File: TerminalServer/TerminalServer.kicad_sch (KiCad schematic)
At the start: 88 parts, among them J1 RJ45_LED, J2 RJ45_LED, J3 RJ45_LED, J4 RJ45_LED, J5 RJ45_LED, J6 RJ45_LED, J7 USB_C_Receptacle_USB2.0_14P, J8 Barrel_Jack_Switch, U1 PIC32MX795F512L-80x-PT, U2 XR32330EBERTR-F, U3 XR32330EBERTR-F, U4 XR32330EBERTR-F, U5 XR32330EBERTR-F, U6 XR32330EBERTR-F, U7 XR32330EBERTR-F, U8 ESP32-WROOM-32D, U9 TPS82130

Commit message: Progress
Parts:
- added C49, C50: 100nF, Capacitor_SMD:C_0603_1608Metric_Pad1.08x0.95mm_HandSolder, symbol Device:C_Small
- added C51: 10uF, Capacitor_SMD:C_1206_3216Metric, symbol Device:C_Small
- added J9: Conn_PIC_ICSP_ICD, Connector_PinHeader_2.54mm:PinHeader_1x06_P2.54mm_Vertical, symbol Connector:Conn_PIC_ICSP_ICD
- added Y1: SIT8103AI-23-33E-8.00000X, Oscillator:Oscillator_SMD_SiT_PQFN-4Pin_3.2x2.5mm, symbol Oscillator:SiT8008xx-2x-xxE
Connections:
- net GND: now also C49.1, C50.1, C51.1, J9.3 (VSS), Y1.2 (GND)
- net PGM_CLOCK: now also J9.5 (PGC/ICSPCLK)
- net PGM_DATA: now also J9.4 (PGD/ICSPDAT)
- net RESET: now also J9.1 (~{MCLR}/VPP)
- net VDD: now also C49.2, C50.2, C51.2, J9.2 (VDD), Y1.4 (Vdd)
- net CLOCK: now reaches U1.63 (RC12/OSC1/CLK)
- net CLOCK: now also Y1.3 (OUT)
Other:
- note added: "TODO ==== 1. Clock for PIC32 2. ICSP for ESP32 3. Check USB C PD resistors 4. Add I2C EEPROM 5. Passives for ESP32"

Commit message: Almost complete
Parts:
- removed NT1, NT2: NetTie_2, NetTie:NetTie-2_SMD_Pad2.0mm, symbol Device:NetTie_2
- added C52: 100uF/50V, Capacitor_THT:CP_Radial_D8.0mm_P3.50mm, symbol Device:C_Polarized
- added C53: 220uF/16V, Capacitor_THT:CP_Radial_D6.3mm_P2.50mm, symbol Device:C_Polarized
- added C54: 100nF, Capacitor_SMD:C_0603_1608Metric_Pad1.08x0.95mm_HandSolder, symbol Device:C_Small
- added J10: Conn_01x06_Pin, Connector_PinHeader_2.54mm:PinHeader_1x06_P2.54mm_Vertical, symbol Connector:Conn_01x06_Pin
- added LED1: 553-0121F, KiCad:5530121F, symbol 553-0121F:553-0121F
- added R16, R17, R18: 10k, Resistor_SMD:R_0603_1608Metric_Pad0.98x0.95mm_HandSolder, symbol Device:R_Small
- added R19, R20: 100R, Resistor_SMD:R_0603_1608Metric_Pad0.98x0.95mm_HandSolder, symbol Device:R_Small
- added R21, R22: 2k2, Resistor_SMD:R_0603_1608Metric_Pad0.98x0.95mm_HandSolder, symbol Device:R_Small
- added U10: 24LC16, Package_SO:SOIC-8_3.9x4.9mm_P1.27mm, symbol Memory_EEPROM:24LC16
- J8: footprint (none) -> Connector_BarrelJack:BarrelJack_Wuerth_6941xx301002
- J9: now not fitted
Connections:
- net GNDA is gone; now on net GND: C46.1, C47.1, C48.1, R15.2, U9.3 (GND), U9.9 (GND)
- net GND: now also J1.11, J2.11, J2.9, J3.11, J3.9, J4.11, J4.9, J5.11, J5.9, J6.11, J6.9, J8.2, J8.3, C52.2, C53.2, C54.1, J10.3 (Pin_3), LED1.1 (K_1), LED1.3 (K_2), R18.2, U10.1 (A0), U10.2 (A1), U10.3 (A2), U10.4 (GND), U10.7 (WP)
- net SCL: now also R21.1, U10.6 (SCL)
- net SDA: now also R22.1, U10.5 (SDA)
- net VCC: now also C52.1
- net VDD: now also C53.1, C54.2, J10.2 (Pin_2), R16.1, R17.2, R20.1, R21.2, R22.2, U10.8 (VCC)
- net ESP_LED: now reaches U8.23 (IO15)
- net ESP_LED: now also R19.2
- net at U8.24 (IO2): now also R18.1
- net ESP_IO0: now reaches U8.25 (IO0)
- net ESP_IO0: now also J10.6 (Pin_6), R17.1
- net ESP_EN: now reaches U8.3 (EN)
- net ESP_EN: now also J10.1 (Pin_1), R16.2
- net ESP_RX: now reaches U8.34 (RXD0/IO3)
- net ESP_RX: now also J10.5 (Pin_5)
- net ESP_TX: now reaches U8.35 (TXD0/IO1)
- net ESP_TX: now also J10.4 (Pin_4)
- new net: LED1.4 (A_2), R19.1
- new net: LED1.2 (A_1), R20.2
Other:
- note added: "TODO ==== 1. Check USB C PD resistors"
- note removed: "TODO ==== 1. Clock for PIC32 2. ICSP for ESP32 3. Check USB C PD resistors 4. Add I2C EEPROM 5. Passives for ESP32"
- moved on the sheet: H1, H2, H3, H4

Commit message: Added Ethernet and more
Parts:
- removed U8: ESP32-WROOM-32D, RF_Module:ESP32-WROOM-32D, symbol RF_Module:ESP32-WROOM-32D
- added C55: 10uF, Capacitor_SMD:C_0805_2012Metric_Pad1.18x1.45mm_HandSolder, symbol Device:C_Small
- added C56, C57, C58, C59, C60: 100nF, Capacitor_SMD:C_0603_1608Metric_Pad1.08x0.95mm_HandSolder, symbol Device:C_Small
- added D3: 1N5819WS, Diode_SMD:D_SOD-323, symbol Diode:1N5819WS
- added J11: SI-60118-F, SI60118F, symbol SI-60118-F:SI-60118-F
- added J12: Conn_01x08_Pin, Connector_PinHeader_2.54mm:PinHeader_1x08_P2.54mm_Vertical, symbol Connector:Conn_01x08_Pin
- added L1: L_Ferrite, Inductor_SMD:L_0603_1608Metric_Pad1.05x0.95mm_HandSolder, symbol Device:L_Ferrite
- added R23: 10k, Resistor_SMD:R_0603_1608Metric_Pad0.98x0.95mm_HandSolder, symbol Device:R_Small
- added R24: 2k32, Resistor_SMD:R_0603_1608Metric_Pad0.98x0.95mm_HandSolder, symbol Device:R_Small
- added R25, R26, R27, R28: 49R9, Resistor_SMD:R_0603_1608Metric_Pad0.98x0.95mm_HandSolder, symbol Device:R_Small
- added R29, R30: 100R, Resistor_SMD:R_0603_1608Metric_Pad0.98x0.95mm_HandSolder, symbol Device:R_Small
- added SW1: SW_Push, Button_Switch_THT:SW_Tactile_SPST_Angled_PTS645Vx31-2LFS, symbol Switch:SW_Push
- added SW2: SW_SPDT, Button_Switch_THT:SW_Slide_SP3T_Straight_CK_OS103012MU1QP1, symbol Switch:SW_SPDT
- added U11: ENC28J60x-ML, Package_DFN_QFN:QFN-28-1EP_6x6mm_P0.65mm_EP4.25x4.25mm, symbol Interface_Ethernet:ENC28J60x-ML
- added U12: ESP32-S3-WROOM-1, RF_Module:ESP32-S3-WROOM-1, symbol RF_Module:ESP32-S3-WROOM-1
- added Y2: ASEMB-25.000MHZ-LC-T, Oscillator:Oscillator_SMD_SiT_PQFN-4Pin_3.2x2.5mm, symbol Oscillator:SiT8008xx-2x-xxE
- J10: footprint Connector_PinHeader_2.54mm:PinHeader_1x06_P2.54mm_Vertical -> Connector_PinHeader_2.54mm:PinHeader_1x10_P2.54mm_Vertical; symbol Connector:Conn_01x06_Pin -> Connector:Conn_01x10_Pin
- LED1: footprint KiCad:5530121F -> LEDS:5530121F
- Y1: value SIT8103AI-23-33E-8.00000X -> ASEMB-8.000MHZ-LC-T
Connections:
- net WIFI_INT is gone; now on net U3DTR: U1.18 (RE8)
- net WIFI_SEL is gone; now on net U1SHTDN: U1.77 (RD2)
- net ESP_EN: now also U1.17 (RA0/TMS), U12.3 (EN)
- net ESP_IO0: now also U12.27 (IO0)
- net ESP_LED: now also U12.8 (IO15)
- net ESP_RX: now also J10.4 (Pin_4), U12.36 (RXD0); no longer J10.5 (Pin_5)
- net ESP_TX: now also J10.5 (Pin_5), U12.37 (TXD0); no longer J10.4 (Pin_4)
- net GND: now also J10.9 (Pin_9), C55.2, C56.1, C57.1, C58.1, C59.1, C60.1, J11.10 (K_GREEN_1), J11.12 (K_GREEN_2), J11.MH1, J11.MH2, J12.8 (Pin_8), R24.2, SW1.2, U11.14 (VSSTX), U11.17 (VSSPLL), U11.18 (VSSOSC), U11.26 (VSS), U11.7 (VSSRX), U12.1 (GND), U12.40 (GND), U12.41 (GND), Y2.2 (GND)
- net SCL: now also U1.58 (RA2), J12.6 (Pin_6); no longer U1.66 (RA14)
- net SDA: now also U1.59 (RA3), J12.7 (Pin_7); no longer U1.67 (RA15)
- net U1CTS: now also U1.79 (RD12); no longer U1.58 (RA2)
- net U1DSR: now also U1.80 (RD13); no longer U1.51 (RF3)
- net U1DTR: now also U1.81 (RD4); no longer U1.60 (RA4/TDI)
- net U1RTS: now also U1.82 (RD5); no longer U1.61 (RA5/TDO)
- net U1RXLED: now also U1.84 (RD7); no longer U1.95 (RG14/TRD2)
- net U1SHTDN: no longer U1.44 (RB15)
- net U1STATUS: now also U1.78 (RD3); no longer U1.59 (RA3)
- net U1TXLED: now also U1.83 (RD6); no longer U1.96 (RG12/TRD1)
- net U2CTS: now also U1.69 (RD9); no longer U1.38 (RA1//TCK)
- net U2DSR: now also U1.73 (RC13/SOSCI); no longer U1.41 (RB12)
- net U2DTR: now also U1.74 (RC14/SOSCO); no longer U1.42 (RB13)
- net U2RTS: now also U1.76 (RD1); no longer U1.43 (RB14)
- net U2RXLED: now also U1.88 (RF1); no longer U1.93 (RE0)
- net U2SHTDN: now also U1.51 (RF3); no longer U1.34 (RB10)
- net U2STATUS: now also U1.68 (RD8); no longer U1.35 (RB11)
- net U2TXLED: now also U1.87 (RF0); no longer U1.94 (RE1)
- net U3CTS: now also U1.7 (RC2); no longer U1.6 (RC1)
- net U3DSR: now also U1.8 (RC3); no longer U1.7 (RC2)
- net U3DTR: no longer U1.8 (RC3)
- net U3RTS: now also U1.19 (RE9); no longer U1.23 (RB2)
- net U3RXLED: now also U1.94 (RE1); no longer U1.87 (RF0)
- net U3SHTDN: now also U1.5 (RE7); no longer U1.4 (RE6)
- net U3STATUS: now also U1.6 (RC1); no longer U1.5 (RE7)
- net U3TXLED: now also U1.93 (RE0); no longer U1.88 (RF1)
- net U4CTS: now also U1.32 (RB8); no longer U1.28 (RA9)
- net U4DSR: now also U1.33 (RB9); no longer U1.29 (RA10)
- net U4DTR: now also U1.34 (RB10); no longer U1.32 (RB8)
- net U4RTS: now also U1.35 (RB11); no longer U1.33 (RB9)
- net U4RXLED: now also U1.90 (RG0); no longer U1.91 (RA6/TRCLK)
- net U4SHTDN: now also U1.28 (RA9); no longer U1.26 (PGEC2/RB6)
- net U4STATUS: now also U1.29 (RA10); no longer U1.27 (PGED2/RB7)
- net U4TXLED: now also U1.89 (RG1); no longer U1.92 (RA7/TRD3)
- net U5CTS: now also U1.22 (RB3); no longer U1.19 (RE9)
- net U5DSR: now also U1.23 (RB2); no longer U1.20 (RB5)
- net U5DTR: now also U1.26 (PGEC2/RB6); no longer U1.21 (RB4)
- net U5RTS: now also U1.27 (PGED2/RB7); no longer U1.22 (RB3)
- net U5RXLED: now also U1.92 (RA7/TRD3); no longer U1.89 (RG1)
- net U5SHTDN: now also U1.20 (RB5); no longer U1.17 (RA0/TMS)
- net U5STATUS: now also U1.21 (RB4); no longer U1.76 (RD1)
- net U5TXLED: now also U1.91 (RA6/TRCLK); no longer U1.90 (RG0)
- net U6DTR: now also U1.3 (RE5); no longer U1.1 (RG15)
- net U6RTS: now also U1.4 (RE6); no longer U1.3 (RE5)
- net U6RXLED: now also U1.96 (RG12/TRD1); no longer U1.83 (RD6)
- net U6TXLED: now also U1.95 (RG14/TRD2); no longer U1.84 (RD7)
- net VCC: now also D3.1 (K), SW2.2 (B); no longer D1.1 (K), D2.1 (K)
- net VDD: now also C58.2, C59.2, C60.2, J12.1 (Pin_1), L1.1, R23.1, U11.11 (VDDTX), U11.15 (VDDRX), U11.16 (VDDPLL), U11.21 (VDDOSC), U11.24 (VDD), U12.2 (3V3), Y2.4 (Vdd)
- net at R18.1: now also U12.16 (IO46)
- net ESP_SEL: now reaches U1.71 (RD11)
- net ESP_SEL: now also U12.19 (IO11)
- net SCK renamed SPI_SCK
- net SPI_SCK: now also U11.4 (SCK), U12.20 (IO12)
- net SDI renamed SPI_MISO
- net SPI_MISO: now also U11.2 (SO), U12.22 (IO14)
- net SDO renamed SPI_MOSI
- net SPI_MOSI: now also U11.3 (SI), U12.18 (IO10)
- net USB_DM renamed USBD_M
- net USB_DP renamed USBD_P
- new net: U11.19 (OSC1), Y2.3 (OUT)
- new net: C55.1, U11.25 (VCAP)
- new net: J11.9 (A_GREEN_1), R29.1
- new net: J11.11 (A_GREEN_2), R30.1
- new net: D3.2 (A), J10.10 (Pin_10)
- new net: R24.1, U11.10 (RBIAS)
- new net ELEDA: R29.2, U11.23 (LEDA)
- new net ELEDB: R30.2, U11.22 (LEDB)
- new net ENC_INT: U1.67 (RA15), U11.28 (~{INT})
- new net ENC_RESET: U1.61 (RA5/TDO), U11.6 (~{RESET})
- new net ENC_SEL: U1.60 (RA4/TDI), U11.5 (~{CS})
- new net ERX_C: C57.2, R27.1, R28.2
- new net ERX_N: J11.6 (RD-), R28.1, U11.8 (TPIN-)
- new net ERX_P: J11.4 (RD+), R27.2, U11.9 (TPIN+)
- new net ESP_INT: U1.66 (RA14), U12.21 (IO13)
- new net ESP_USB_N: J10.8 (Pin_8), U12.13 (USB_D-)
- new net ESP_USB_P: J10.7 (Pin_7), U12.14 (USB_D+)
- new net ETX_C: C56.2, J11.2 (TCT), L1.2, R25.2, R26.1
- new net ETX_N: J11.3 (TD-), R25.1, U11.12 (TPOUT-)
- new net ETX_P: J11.1 (TD+), R26.2, U11.13 (TPOUT+)
- new net FRES: R23.2, SW1.1, U1.1 (RG15)
- new net GPIO0: J12.2 (Pin_2), U1.41 (RB12)
- new net GPIO1: J12.3 (Pin_3), U1.42 (RB13)
- new net GPIO2: J12.4 (Pin_4), U1.43 (RB14)
- new net GPIO3: J12.5 (Pin_5), U1.38 (RA1//TCK)
- new net SWIN: D1.1 (K), D2.1 (K), SW2.3 (C)
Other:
- moved on the sheet: J9, R16, R17, R18

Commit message: Added 4-led module
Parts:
- removed LED1: 553-0121F, LEDS:5530121F, symbol 553-0121F:553-0121F
- removed R19, R20: 100R, Resistor_SMD:R_0603_1608Metric_Pad0.98x0.95mm_HandSolder, symbol Device:R_Small
- added D4: XL-DZ234SYGD-4, XINGLIGHT:XL-DZ234SYGD-4, symbol XINGLIGHT:XL-DZ234SYGD/4
- added R31, R32, R33, R34: 100R, Resistor_SMD:R_0603_1608Metric_Pad0.98x0.95mm_HandSolder, symbol Device:R_Small
- J10: value Conn_01x06_Pin -> Conn_01x10_Pin
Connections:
- net GND: now also D4.1 (LED_K1), D4.3 (LED_K2), D4.5 (LED_K3), D4.7 (LED_K4)
- net LED2: now reaches U12.10 (IO17)
- net LED2: now also R32.1
- net LED3: now reaches U12.11 (IO18)
- net LED3: now also R33.1
- net LED4: now reaches U12.12 (IO8)
- net LED4: now also R34.1
- net LED1: now reaches U12.9 (IO16)
- net LED1: now also R31.1
- new net: D4.2 (LED_A1), R31.2
- new net: D4.4 (LED_A2), R32.2
- new net: D4.6 (LED_A3), R33.2
- new net: D4.8 (LED_A4), R34.2

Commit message: Almost complete
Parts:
- D1, D2, D3: value 1N5819WS -> V8PAN50-M3/I; footprint Diode_SMD:D_SOD-323 -> Diode_SMD:Vishay_SMPA
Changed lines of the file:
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@@
 			)
 		)
-		(property "Value" "1N5819WS"
+		(property "Value" "V8PAN50-M3/I"
 			(at 82.8675 266.7 0)
 			(effects
@@
 			)
 		)
-		(property "Footprint" "Diode_SMD:D_SOD-323"
+		(property "Footprint" "Diode_SMD:Vishay_SMPA"
 			(at 82.55 274.955 0)
 			(effects
@@
 			)
 		)
-		(property "Value" "1N5819WS"
+		(property "Value" "V8PAN50-M3/I"
 			(at 211.1375 232.41 0)
 			(effects
@@
 			)
 		)
-		(property "Footprint" "Diode_SMD:D_SOD-323"
+		(property "Footprint" "Diode_SMD:Vishay_SMPA"
 			(at 210.82 240.665 0)
 			(effects
@@
 			)
 		)
-		(property "Value" "1N5819WS"
+		(property "Value" "V8PAN50-M3/I"
 			(at 108.2675 210.82 0)
 			(effects
@@
 			)
 		)
-		(property "Footprint" "Diode_SMD:D_SOD-323"
+		(property "Footprint" "Diode_SMD:Vishay_SMPA"
 			(at 107.95 219.075 0)
 			(effects

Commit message: Added SD card
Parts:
- added J13: Micro_SD_Card, MolexSD:503182-1852_MOL, symbol Connector:Micro_SD_Card
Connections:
- net ESP_USB_N: now also J10.7 (Pin_7); no longer J10.8 (Pin_8)
- net ESP_USB_P: now also J10.8 (Pin_8); no longer J10.7 (Pin_7)
- net GND: now also J13.6 (VSS)
- net SPI_MISO: now also J13.7 (DAT0)
- net SPI_MOSI: now also J13.3 (CMD)
- net SPI_SCK: now also J13.5 (CLK)
- net VDD: now also J13.4 (VDD)
- net SD_CS: now reaches U1.44 (RB15)
- net SD_CS: now also J13.2 (DAT3/CD)

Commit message: Final cleanup
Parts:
- removed D4: XL-DZ234SYGD-4, XINGLIGHT:XL-DZ234SYGD-4, symbol XINGLIGHT:XL-DZ234SYGD/4
- removed J13: Micro_SD_Card, MolexSD:503182-1852_MOL, symbol Connector:Micro_SD_Card
- removed J7: USB_C_Receptacle_USB2.0_14P, Connector_USB:USB_C_Receptacle_GCT_USB4105-xx-A_16P_TopMnt_Horizontal, symbol Connector:USB_C_Receptacle_USB2.0_14P
- removed R34: 100R, Resistor_SMD:R_0603_1608Metric_Pad0.98x0.95mm_HandSolder, symbol Device:R_Small
- added D4: 564-0100-132F, 5640100222F, symbol 564-0100-132F:564-0100-132F
- added J13: 503398-1892, 5033981892, symbol 503398-1892:503398-1892
- added J7: USB_B, Connector_USB:USB_B_OST_USB-B1HSxx_Horizontal, symbol Connector:USB_B
- U1: Mouser (none) -> 579-PIC32MX795F512
- U2, U3, U4, U5, U6, U7: Mouser (none) -> 701-XR32330EBERTR-F
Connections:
- net GND: now also D4.1 (K_POSITION_3), D4.3 (K_POSITION_2), D4.5 (K_POSITION_1), J13.11, J13.12, J13.13, J13.14, J13.6 (VSS), J7.4 (GND), J7.SH (Shield)
- net SD_CS: now also J13.2 (CD/DAT3)
- net SPI_MISO: now also J13.7 (DAT0)
- net SPI_MOSI: now also J13.3 (CMD)
- net SPI_SCK: now also J13.5 (CLK)
- net USBD_M: now also J7.2 (D-)
- net USBD_P: now also J7.3 (D+)
- net USB_VBUS: now also J7.1 (VBUS)
- net VDD: now also J13.4 (VDD)
- net at R31.2: now also D4.2 (A_POSITION_3)
- net at R32.2: now also D4.4 (A_POSITION_2)
- net at R33.2: now also D4.6 (A_POSITION_1)
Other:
- moved on the sheet: C52, D1, R31, R32, R33

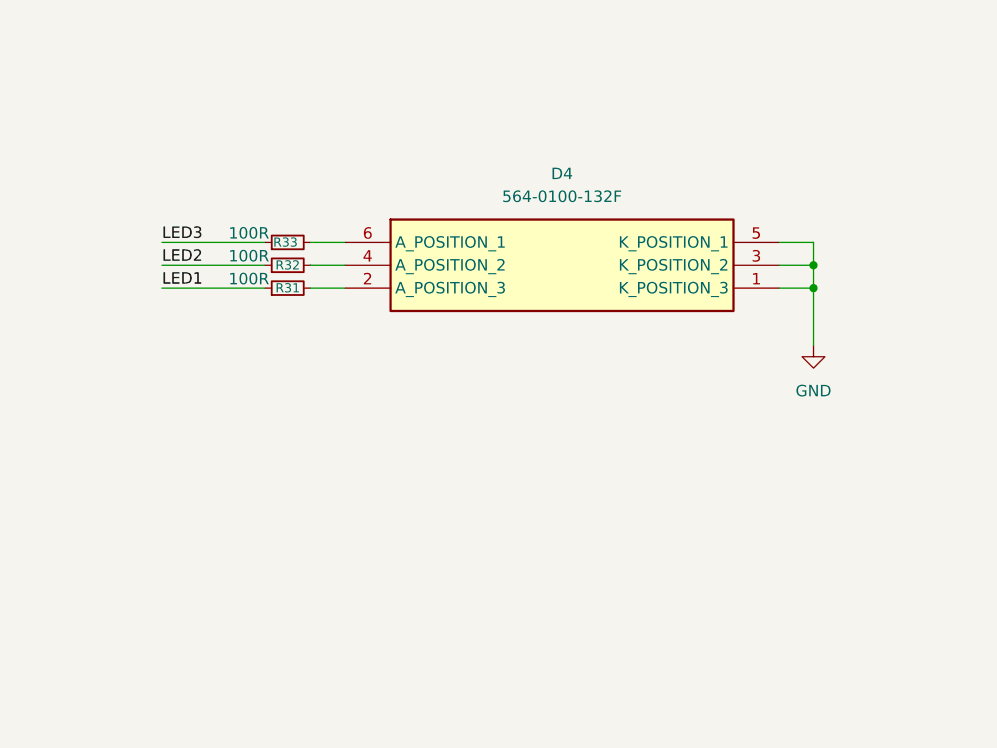
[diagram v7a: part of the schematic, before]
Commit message: Reverted to quad LED
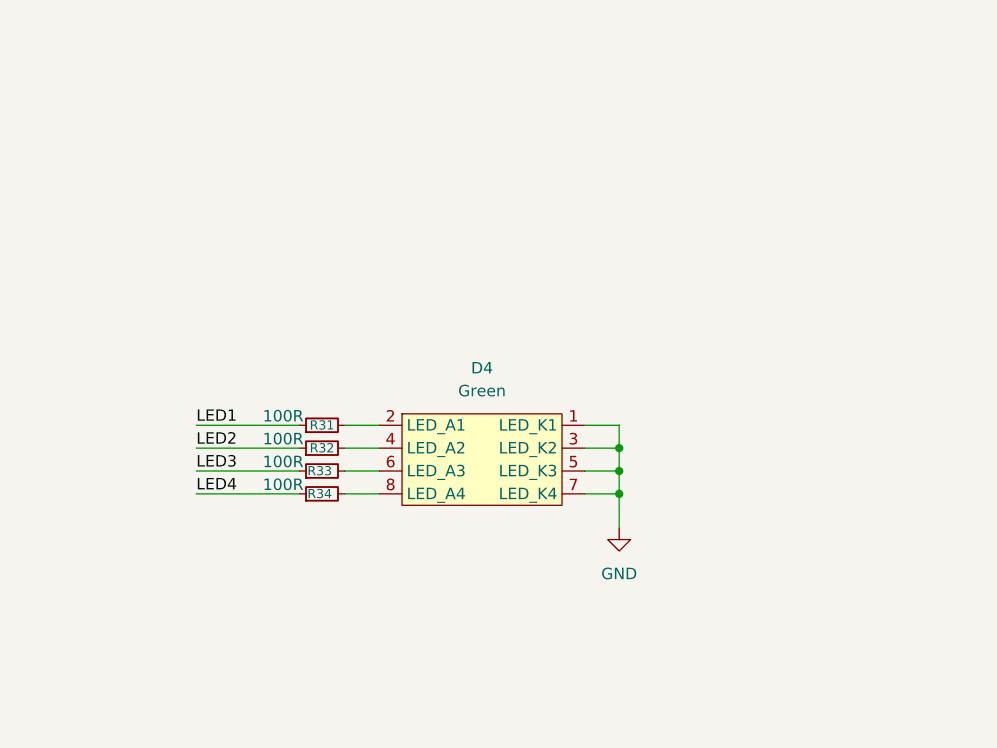
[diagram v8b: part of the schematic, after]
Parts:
- removed D4: 564-0100-132F, 5640100222F, symbol 564-0100-132F:564-0100-132F
- added D4: Green, XINGLIGHT:XL-DZ234SYGD-4, symbol XINGLIGHT:XL-DZ234SYGD/4
- added R34: 100R, Resistor_SMD:R_0603_1608Metric_Pad0.98x0.95mm_HandSolder, symbol Device:R_Small
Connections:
- net GND: now also D4.1 (LED_K1), D4.3 (LED_K2), D4.5 (LED_K3), D4.7 (LED_K4)
- net LED4: now also R34.1
- net at R31.2: now also D4.2 (LED_A1)
- net at R32.2: now also D4.4 (LED_A2)
- net at R33.2: now also D4.6 (LED_A3)
- new net: D4.8 (LED_A4), R34.2
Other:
- moved on the sheet: R31, R32, R33
